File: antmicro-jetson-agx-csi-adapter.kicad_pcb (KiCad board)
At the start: 4 copper layers, 73.6 x 41 mm, 98 parts, among them IC1 MAX1708EEE+, J1 QTH-060-03-L-D-A, J2 WE_68715014522_ONE-SIDE, J3 WE_68715014022, J4 BM04B-SRSS-TB-LF-SN, J5 SM06B-SRSS-TB(LF)(SN), J6 SM09B-SRSS-TB(LF)(SN), Q1 BSS138AKA, U1 PCA9547BS,118, U2 NTS0102DP

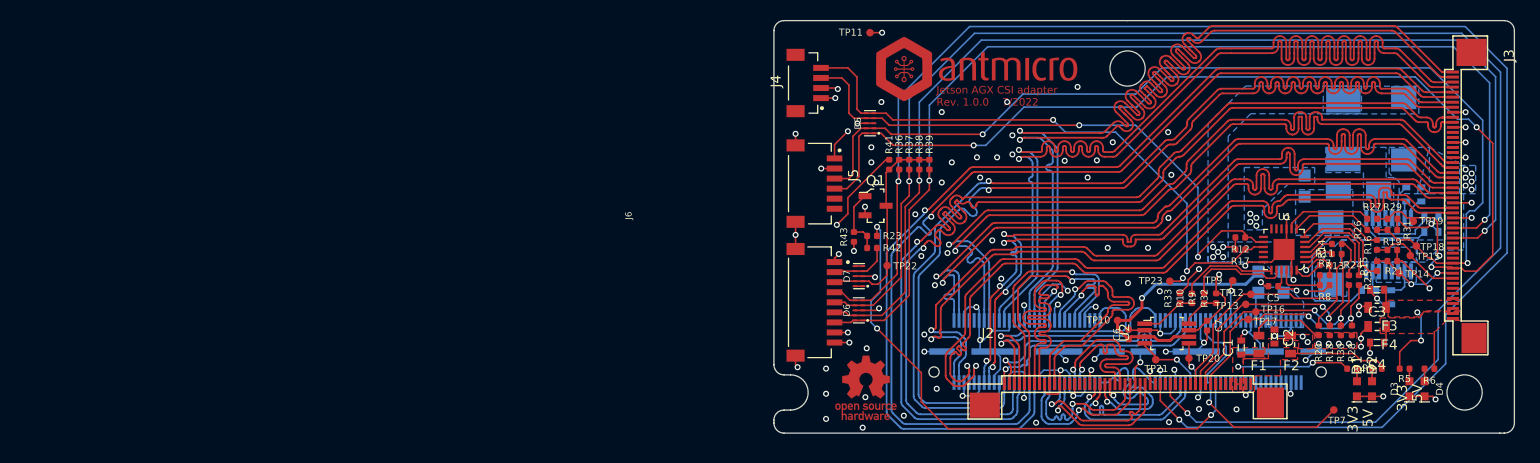
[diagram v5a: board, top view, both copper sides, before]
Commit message: Cleaned up silk screen
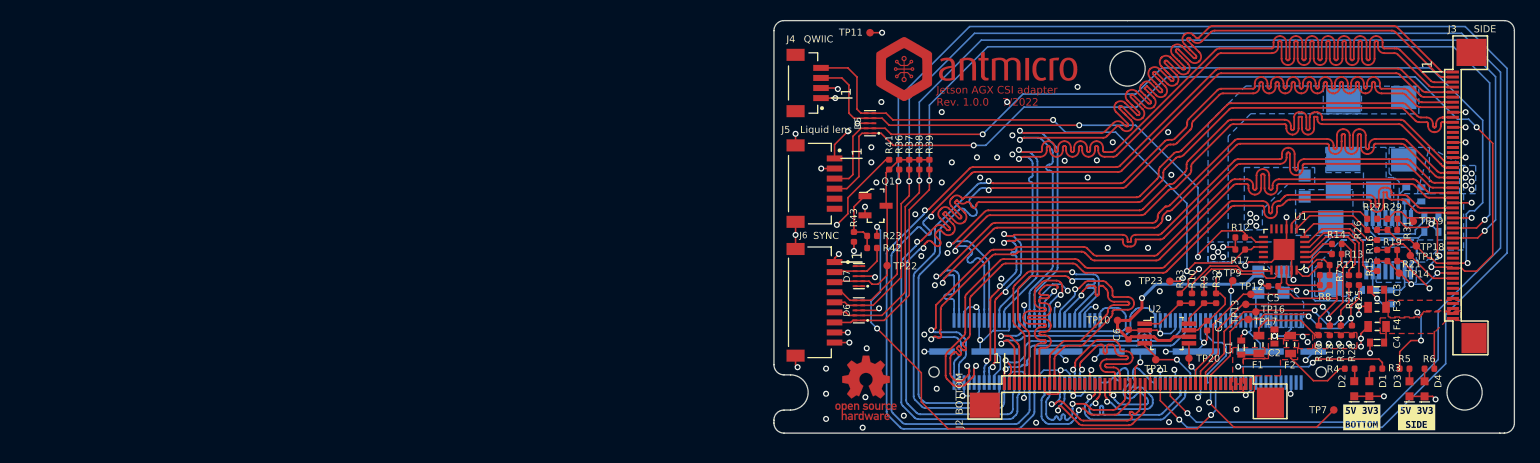
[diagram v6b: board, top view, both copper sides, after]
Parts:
- added kibuzzard-62DE644D: G***, kibuzzard-62DE644D, F.Cu at (178.7, 107.4)
- added kibuzzard-62DE6453: G***, kibuzzard-62DE6453, F.Cu at (173.3, 107.4)
- moved R4 2.70 mm to (172.1, 102.6), turned to 0 degrees
- moved R3 2.52 mm to (174.8, 102.6), turned to 180 degrees
- moved D2 1.77 mm to (172.5, 104.6)
- moved D1 1.23 mm to (174.0, 104.6)
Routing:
- net /Interface/3V3_FFC_B: track 13.4 -> 17.5 mm
- net /Interface/5V_FFC_B: track 9.89 -> 7.25 mm
- net /Interface/CSI7_D0_P: track 23.8 -> 23.2 mm
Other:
- board text added: "1"
- board text added: "BOTTOM"
- board text added: "Liquid lens"
- board text added: "QWIIC"
- board text added: "SIDE"
- board text added: "SYNC"
- board text removed: "3V3"
- board text removed: "5V"

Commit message: Added fuses for aux connectors
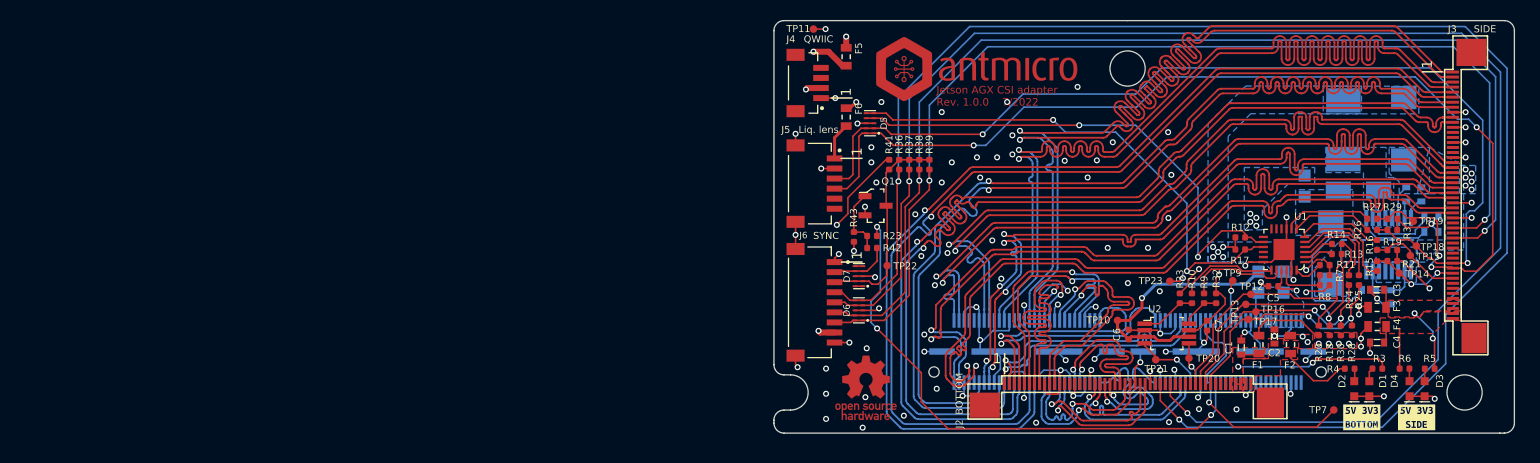
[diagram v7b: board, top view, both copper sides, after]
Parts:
- added F5: 04671.25NR, antmicro-footprints:0603-Fuse-Littelfuse-0467, F.Cu at (122.0, 71.6)
- added F6: 04671.25NR, antmicro-footprints:0603-Fuse-Littelfuse-0467, F.Cu at (122.0, 77.6)
- moved TP11 5.63 mm to (118.8, 68.9)
- moved R5 2.50 mm to (180.0, 102.6), turned to 180 degrees
- moved R6 2.48 mm to (177.5, 102.6), turned to 0 degrees
- moved D3 1.51 mm to (179.5, 104.6)
- moved D4 1.49 mm to (178.0, 104.6)
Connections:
- J4 pad 2: +3V3 -> /Auxiliary/3V3_AUX_F
- J5 pad 1: +5V -> /Auxiliary/5V_LL
- J6 pad 8: +3V3 -> /Auxiliary/3V3_AUX_F
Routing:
- net /Auxiliary/AUX_I2C_SCL: track 59.2 -> 50.9 mm
- net /Auxiliary/AUX_I2C_SDA: track 58.9 -> 51.1 mm
- net /Auxiliary/3V3_AUX_F: track 0.00 -> 7.04 mm, vias 0 -> 3
- net /Auxiliary/5V_LL: track 0.00 -> 3.70 mm
- net +5V: track 6.97 -> 4.97 mm
- net +3V3: track 56.7 -> 54.8 mm, vias 21 -> 20
- net /Interface/3V3_FFC_S: track 8.79 -> 7.89 mm
- added copper zone on In2.Cu, net /Auxiliary/3V3_AUX_F
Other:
- board text added: "Liq. lens"
- board text removed: "Liquid lens"

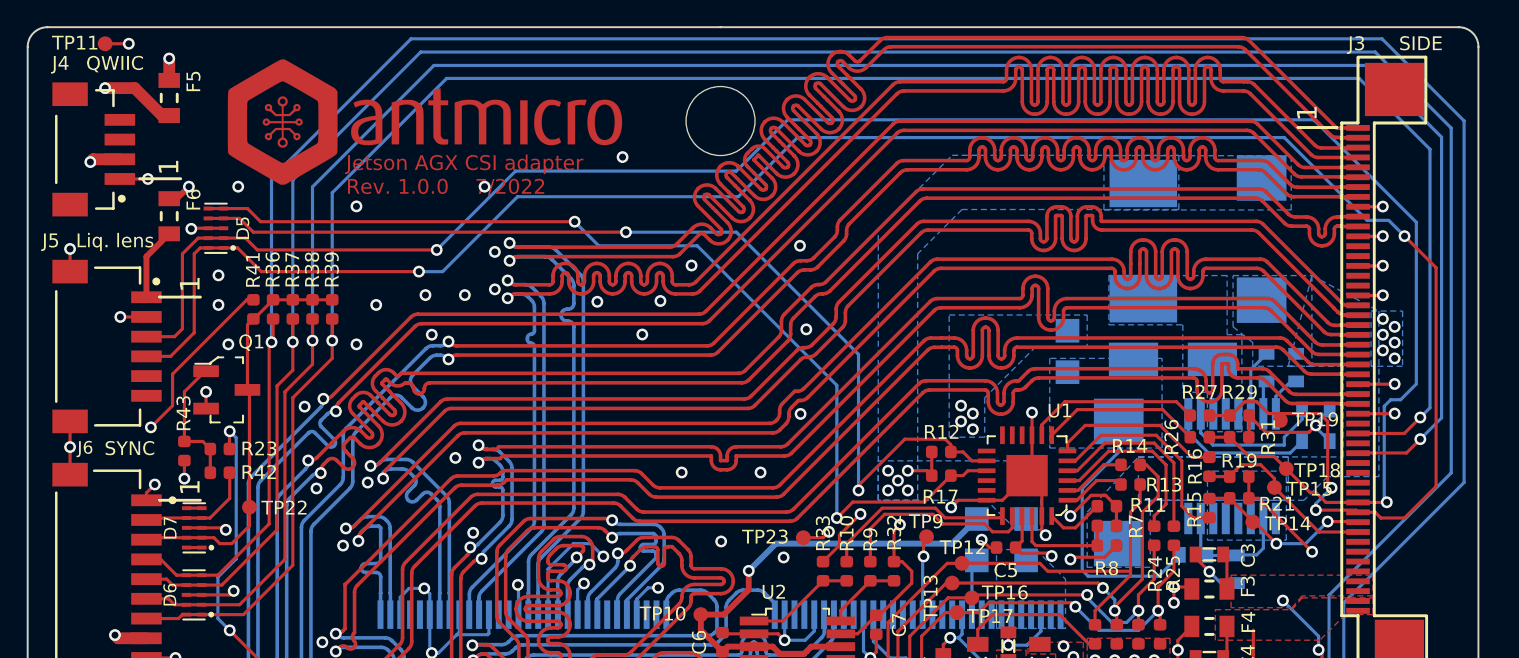
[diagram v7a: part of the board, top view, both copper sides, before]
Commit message: Merged zones and minor net fixes
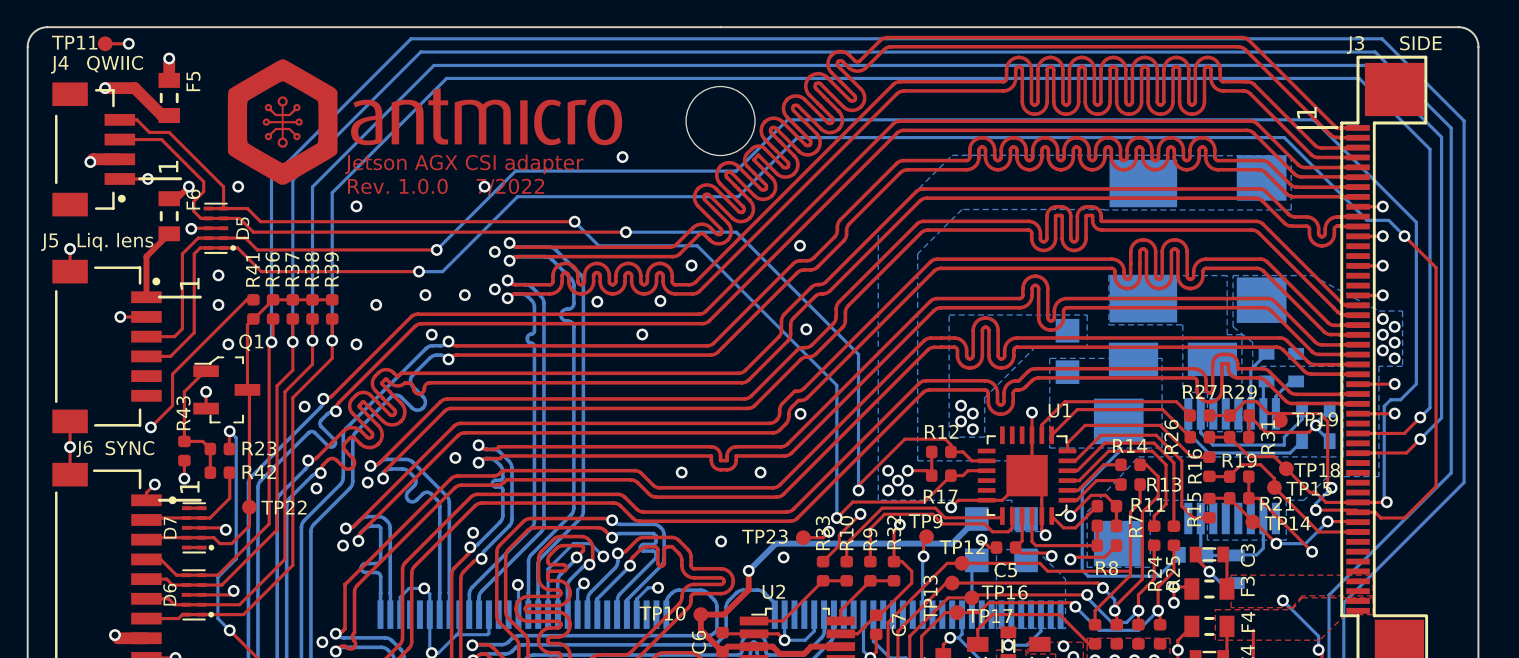
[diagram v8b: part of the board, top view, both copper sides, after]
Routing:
- net /Auxiliary/AUX_I2C_SCL: track 50.9 -> 58.7 mm
- net /Auxiliary/AUX_I2C_SDA: track 51.1 -> 58.9 mm
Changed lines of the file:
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@@
   (segment (start 162.3 90.75) (end 161.685 90.75) (width 0.16) (layer "F.Cu") (net 63))
   (segment (start 126.667895 77.867895) (end 126 77.2) (width 0.16) (layer "F.Cu") (net 63))
+  (segment (start 120.39 72.7) (end 121.03 73.34) (width 0.16) (layer "F.Cu") (net 63))
   (segment (start 160.345 92.09) (end 161.685 90.75) (width 0.16) (layer "F.Cu") (net 63))
   (segment (start 126 77.2) (end 124.7875 77.2) (width 0.16) (layer "F.Cu") (net 63))
@@
   (segment (start 124.7875 77.2) (end 124.0125 77.2) (width 0.16) (layer "F.Cu") (net 63))
   (segment (start 162.55 90.5) (end 162.3 90.75) (width 0.16) (layer "F.Cu") (net 63))
+  (segment (start 122.03 73.34) (end 124.7875 76.0975) (width 0.16) (layer "F.Cu") (net 63))
   (segment (start 155.9 92.9) (end 156.71 92.09) (width 0.16) (layer "F.Cu") (net 63))
+  (segment (start 119.525 72.7) (end 120.39 72.7) (width 0.16) (layer "F.Cu") (net 63))
+  (segment (start 124.7875 76.0975) (end 124.7875 77.2) (width 0.16) (layer "F.Cu") (net 63))
+  (segment (start 121.03 73.34) (end 122.03 73.34) (width 0.16) (layer "F.Cu") (net 63))
   (via (at 155.9 92.9) (size 0.6) (drill 0.35) (layers "F.Cu" "B.Cu") (net 63))
   (via (at 142.6 77.867895) (size 0.6) (drill 0.35) (layers "F.Cu" "B.Cu") (net 63))
@@
   (segment (start 143.822105 79.09) (end 142.6 77.867895) (width 0.16) (layer "B.Cu") (net 63))
   (segment (start 148.82 79.09) (end 143.822105 79.09) (width 0.16) (layer "B.Cu") (net 63))
+  (segment (start 123.64 77.7) (end 123.28 77.34) (width 0.16) (layer "F.Cu") (net 64))
   (segment (start 162.75 90) (end 162.3 89.55) (width 0.16) (layer "F.Cu") (net 64))
   (segment (start 126.297395 78.397395) (end 125.6 77.7) (width 0.16) (layer "F.Cu") (net 64))
   (segment (start 161.685 89.185) (end 161.4 88.9) (width 0.16) (layer "F.Cu") (net 64))
   (segment (start 145.197395 78.397395) (end 126.297395 78.397395) (width 0.16) (layer "F.Cu") (net 64))
+  (segment (start 124.0125 77.7) (end 123.64 77.7) (width 0.16) (layer "F.Cu") (net 64))
   (segment (start 161.685 89.55) (end 161.685 89.185) (width 0.16) (layer "F.Cu") (net 64))
+  (segment (start 123.28 77.34) (end 123.28 76.84) (width 0.16) (layer "F.Cu") (net 64))
+  (segment (start 123.78 76.34) (end 123.78 75.84) (width 0.16) (layer "F.Cu") (net 64))
   (segment (start 145.2 78.4) (end 145.197395 78.397395) (width 0.16) (layer "F.Cu") (net 64))
   (segment (start 163.5 90) (end 162.75 90) (width 0.16) (layer "F.Cu") (net 64))
   (segment (start 124.0125 77.7) (end 124.7875 77.7) (width 0.16) (layer "F.Cu") (net 64))
   (segment (start 162.3 89.55) (end 161.685 89.55) (width 0.16) (layer "F.Cu") (net 64))
+  (segment (start 123.28 76.84) (end 123.78 76.34) (width 0.16) (layer "F.Cu") (net 64))
+  (segment (start 121.64 73.7) (end 119.525 73.7) (width 0.16) (layer "F.Cu") (net 64))
   (segment (start 125.6 77.7) (end 124.7875 77.7) (width 0.16) (layer "F.Cu") (net 64))
   (segment (start 157 91.250466) (end 157 91.5) (width 0.16) (layer "F.Cu") (net 64))
   (segment (start 159.350466 88.9) (end 157 91.250466) (width 0.16) (layer "F.Cu") (net 64))
   (segment (start 161.4 88.9) (end 159.350466 88.9) (width 0.16) (layer "F.Cu") (net 64))
+  (segment (start 123.78 75.84) (end 121.64 73.7) (width 0.16) (layer "F.Cu") (net 64))
   (via (at 157 91.5) (size 0.6) (drill 0.35) (layers "F.Cu" "B.Cu") (net 64))
   (via (at 145.2 78.4) (size 0.6) (drill 0.35) (layers "F.Cu" "B.Cu") (net 64))
@@
     )
   )
-  (zone (net 1) (net_name "GND") (layer "B.Cu") (hatch edge 0.508)
-    (connect_pads (clearance 0))
-    (min_thickness 0.254) (filled_areas_thickness no)
-    (fill yes (thermal_gap 0.508) (thermal_bridge_width 10))
-    (polygon
-      (pts
-        (xy 178.8 92)
-        (xy 171.8 92)
-        (xy 171.8 95.4)
-        (xy 168.6 95.4)
-        (xy 168.6 92.6)
-        (xy 171.2 89.8)
-        (xy 178.8 89.8)
-      )
-    )
-  )
-  (zone (net 1) (net_name "GND") (layer "B.Cu") (hatch edge 0.508)
-    (connect_pads (clearance 0))
-    (min_thickness 0.254) (filled_areas_thickness no)
-    (fill yes (thermal_gap 0.508) (thermal_bridge_width 10))
-    (polygon
-      (pts
-        (xy 180 85.2)
-        (xy 177 85.2)
-        (xy 177 84)
-        (xy 176 83.2)
-        (xy 176 80.6)
-        (xy 180 80.6)
-      )
-    )
-  )
-  (zone (net 2) (net_name "+3V3") (layer "B.Cu") (hatch edge 0.508)
-    (priority 1)
-    (connect_pads (clearance 0))
-    (min_thickness 0.254) (filled_areas_thickness no)
-    (fill yes (thermal_gap 0.508) (thermal_bridge_width 10))
-    (polygon
-      (pts
-        (xy 173.25 77.25)
-        (xy 162.25 77.25)
-        (xy 160 79.5)
-        (xy 160 92)
-        (xy 158 92)
-        (xy 158 78.25)
-        (xy 161.75 74.5)
-        (xy 173.25 74.5)
-      )
-    )
-  )
   (zone (net 162) (net_name "/Auxiliary/5V_C") (layer "B.Cu") (hatch edge 0.508)
     (connect_pads (clearance 0))
@@
     (polygon
       (pts
+        (xy 183.4 82.4)
+        (xy 184.6 82.4)
         (xy 184.6 85.2)
-        (xy 183 85.2)
-        (xy 183 82.4)
-        (xy 184.6 82.4)
+        (xy 183.4 85.2)
+        (xy 183.4 90.8)
+        (xy 180.8 90.8)
+        (xy 179.6 92)
+        (xy 178.7 92)
+        (xy 178.7 94.021)
+        (xy 174.7 94.021)
+        (xy 174.7 92)
+        (xy 171.8 92)
+        (xy 171.8 95.4)
+        (xy 168.6 95.4)
+        (xy 168.6 92.6)
+        (xy 171.2 89.8)
+        (xy 181.6 89.8)
+        (xy 181.6 85.2)
+        (xy 177 85.2)
+        (xy 177 84)
+        (xy 176 83.2)
+        (xy 176 80.6)
+        (xy 180 80.6)
       )
     )
@@
   (zone (net 168) (net_name "/Interface/3V3_CONN") (layer "B.Cu") (hatch edge 0.508)
     (connect_pads (clearance 0))
-    (min_thickness 0.254) (filled_areas_thickness no)
+    (min_thickness 0.1) (filled_areas_thickness no)
     (fill yes (thermal_gap 0.508) (thermal_bridge_width 10))
     (polygon
@@
         (xy 164 94.5)
         (xy 166 94.5)
-      )
-    )
-  )
-  (zone (net 1) (net_name "GND") (layer "B.Cu") (hatch edge 0.508)
-    (priority 1)
-    (connect_pads (clearance 0))
-    (min_thickness 0.2) (filled_areas_thickness no)
-    (fill yes (thermal_gap 0.2) (thermal_bridge_width 10))
-    (polygon
-      (pts
-        (xy 178.7 94.021)
-        (xy 178.7 90.521)
-        (xy 174.7 90.521)
-        (xy 174.7 94.021)
       )
     )
@@
     (priority 1)
     (connect_pads (clearance 0))
-    (min_thickness 0.2) (filled_areas_thickness no)
-    (fill yes (thermal_gap 0.2) (thermal_bridge_width 10) (smoothing chamfer) (radius 0.5))
-    (polygon
-      (pts
-        (xy 178.95 77.271)
-        (xy 178.95 74.521)
-        (xy 169.45 74.521)
-        (xy 169.45 77.271)
-      )
-    )
-  )
-  (zone (net 2) (net_name "+3V3") (layer "B.Cu") (hatch edge 0.508)
-    (priority 1)
-    (connect_pads (clearance 0))
     (min_thickness 0.254) (filled_areas_thickness no)
     (fill yes (thermal_gap 0.508) (thermal_bridge_width 10))
     (polygon
       (pts
-        (xy 166.25 93.5)
-        (xy 165 93.5)
-        (xy 163.5 92)
+        (xy 173.25 74.521)
+        (xy 178.95 74.521)
+        (xy 178.95 77.271)
+        (xy 169.45 77.271)
+        (xy 169.45 77.25)
+        (xy 162.25 77.25)
+        (xy 160 79.5)
+        (xy 160 90)
+        (xy 166.25 90)
+        (xy 166.25 93.59)
+        (xy 164.78 93.59)
+        (xy 164.78 92)
         (xy 158 92)
-        (xy 158 90)
-        (xy 166.25 90)
+        (xy 158 78.25)
+        (xy 161.75 74.5)
+        (xy 173.25 74.5)
       )
     )
-  )
-  (zone (net 1) (net_name "GND") (layer "B.Cu") (hatch edge 0.508)
-    (connect_pads (clearance 0))
-    (min_thickness 0.254) (filled_areas_thickness no)
-    (fill yes (thermal_gap 0.508) (thermal_bridge_width 10))
-    (polygon
-      (pts
-        (xy 183.4 82.4)
-        (xy 183.4 90.8)
-        (xy 180.8 90.8)
-        (xy 179.6 92)
-        (xy 171.2 92)
-        (xy 171.2 89.8)
-        (xy 181.6 89.8)
-        (xy 181.6 85.2)
-        (xy 178.8 85.2)
-        (xy 180 80.6)
-      )
-    )
